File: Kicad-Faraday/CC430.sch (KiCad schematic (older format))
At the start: 32 parts, among them P2 DNP, U1 CC430F6137, U14 0915BM15A0001E, X1 ST3215SB32768H5HPWAA, X2 ABM8G-26.000MHZ-18-D2Y-T

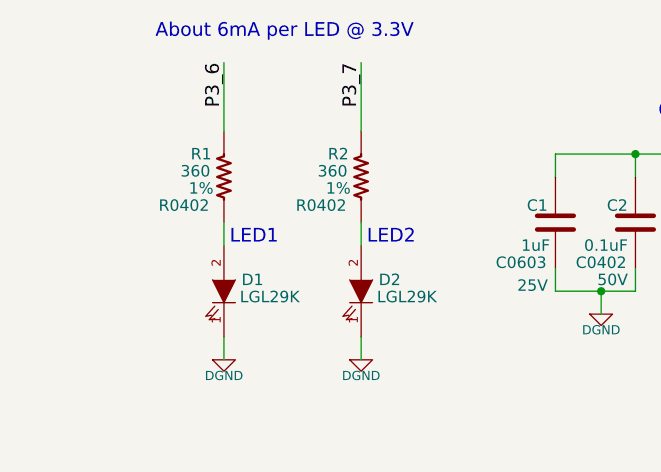
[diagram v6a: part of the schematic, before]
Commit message: Cleaned up a few connections on the schematic to make sure wire junctions were used. Also added a few notes such as LED color. Output new PDF of Schematics and updated Rev to Rev D1 for PCB:NG
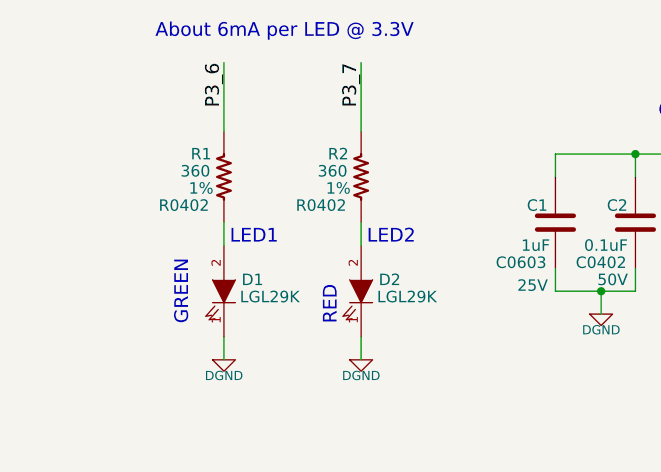
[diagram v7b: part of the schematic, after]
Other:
- note added: "GREEN"
- note added: "RED"
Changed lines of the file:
@@
 Sheet 3 11
 Title "Faraday Wireless Node"
-Date "14 nov 2016"
-Rev "C"
+Date "15 nov 2016"
+Rev "D1"
 Comp "FaradayRF"
 Comment1 "www.FaradayRF.com"
@@
 56 10 04 A1 18 0C 2B 08 82 50 0C 86 15 04 41 28 06 C3 0A 82 20 14 83 61 05 41 10 8A C1 B0 82 20
 08 C5 60 58 41 10 84 62 30 AC 20 08 42 31 FF 0F 83 E1 BA 3C 1C 59 E8 E4 00 00 00 00 49 45 4E 44
-AE 42 60 82 22 $EndBitmap
+AE 42 60 82 BD $EndBitmap
 EndData
 $EndBitmap
@@
 Wire Wire Line
 	5200 1950 5200 2050
+Text Notes 1100 9850 1    60   ~ 0
+GREEN
+Text Notes 1750 9850 1    60   ~ 0
+RED
 $EndSCHEMATC
